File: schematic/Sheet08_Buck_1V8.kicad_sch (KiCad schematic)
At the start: 15 parts, among them U6 ISL70003ASEH

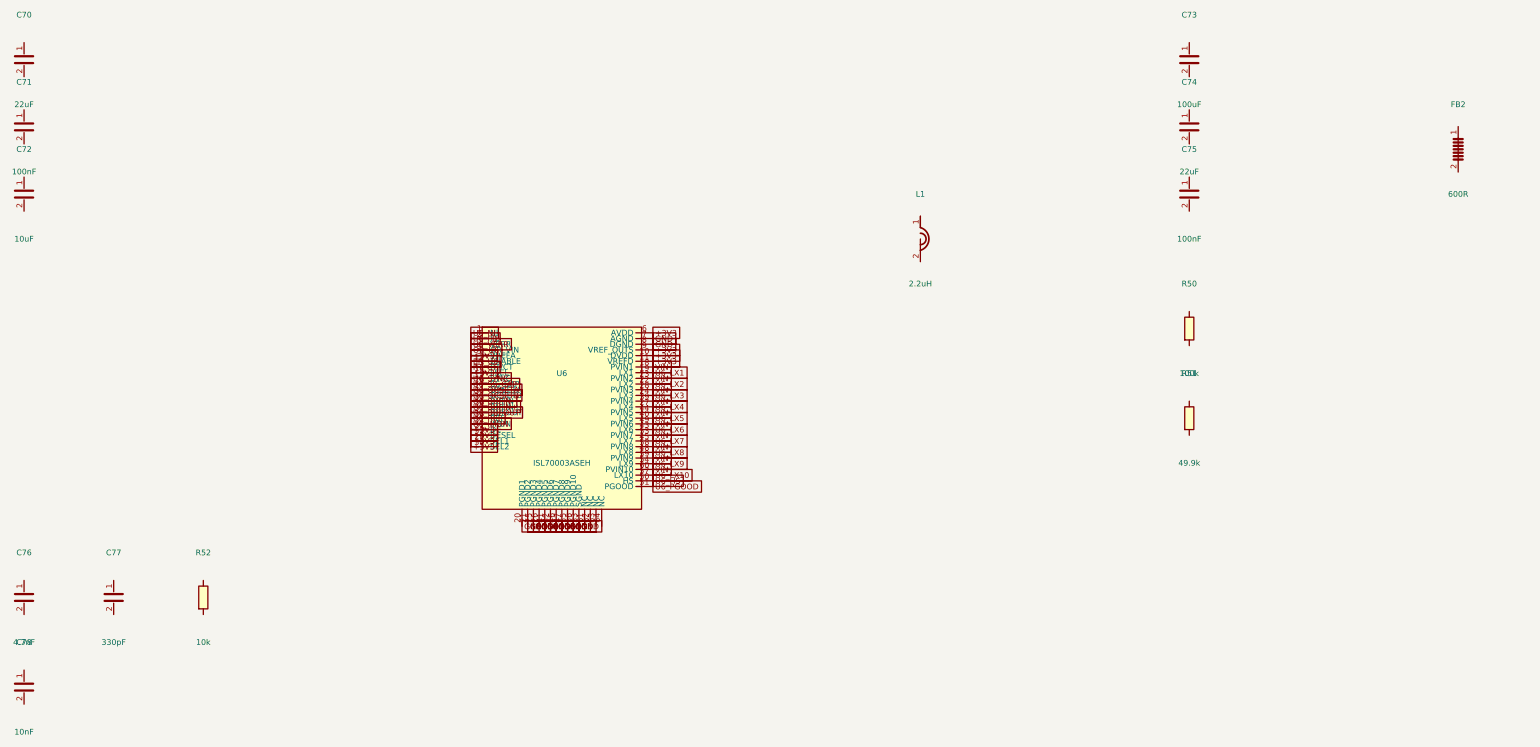
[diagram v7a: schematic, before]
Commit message: feat: connect ALL passive components and fix clock routing
- Added PASSIVE_TOPOLOGY dict mapping 139 passives to their nets
- Passive pin endpoints now get global_labels (was 0 connected, now 138)
- R38 intentionally GND-GND (RECAL_EN pull-down)
- Fixed LMK clock output mapping: CLKout0→ADC_CLK_P, CLKout2→FPGA_REFCLK_P, etc.
- Fixed TPS7H5001-SP SYNC pin collision with LMX_SYNC
- Total connections: 867 pins (up from 641)
- Cross-sheet nets: 52
- Power rails: VIN(33), +3V3(98), GND(228) all with decoupling
- JESD204C: U1↔U2 on 4 lanes ✓
- SPI: U1↔U2↔U3↔U4 ✓
- Clock: LMK→ADC (CLK+SYSREF), LMK→FPGA (REF+SPW) ✓
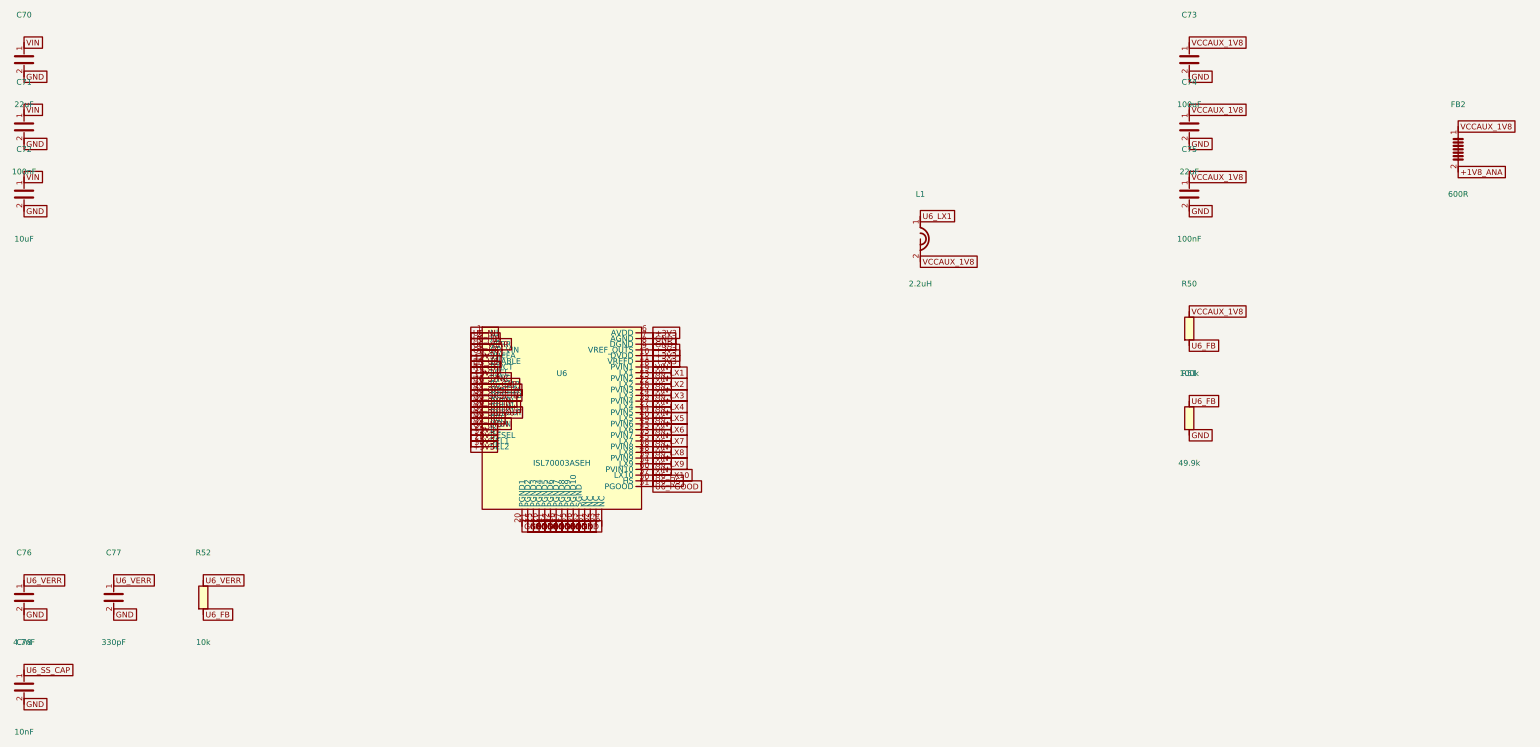
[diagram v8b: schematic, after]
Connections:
- net GND: now also C70.2, C71.2, C72.2, C73.2, C74.2, C75.2, C76.2, C77.2, C78.2, R51.2
- net U6_FB: now also R50.2, R51.1, R52.2
- net U6_LX1: now also L1.1
- net U6_SS_CAP: now also C78.1
- net U6_VERR: now also C76.1, C77.1, R52.1
- net VIN: now also C70.1, C71.1, C72.1
- net VCCAUX_1V8: now reaches C73.1
- net VCCAUX_1V8: now also C74.1, C75.1, FB2.1, L1.2, R50.1
- net +1V8_ANA: now reaches FB2.2
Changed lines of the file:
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@@
   (global_label "GND" (at 202.5400 144.1300 0) (effects (font (size 1.27 1.27))))
   (global_label "GND" (at 203.8100 144.1300 0) (effects (font (size 1.27 1.27))))
+  (global_label "VIN" (at 80.0000 36.1900 0) (effects (font (size 1.27 1.27))))
+  (global_label "GND" (at 80.0000 43.8100 0) (effects (font (size 1.27 1.27))))
+  (global_label "VIN" (at 80.0000 51.1900 0) (effects (font (size 1.27 1.27))))
+  (global_label "GND" (at 80.0000 58.8100 0) (effects (font (size 1.27 1.27))))
+  (global_label "VIN" (at 80.0000 66.1900 0) (effects (font (size 1.27 1.27))))
+  (global_label "GND" (at 80.0000 73.8100 0) (effects (font (size 1.27 1.27))))
+  (global_label "U6_LX1" (at 280.0000 74.9200 0) (effects (font (size 1.27 1.27))))
+  (global_label "VCCAUX_1V8" (at 280.0000 85.0800 0) (effects (font (size 1.27 1.27))))
+  (global_label "VCCAUX_1V8" (at 340.0000 36.1900 0) (effects (font (size 1.27 1.27))))
+  (global_label "GND" (at 340.0000 43.8100 0) (effects (font (size 1.27 1.27))))
+  (global_label "VCCAUX_1V8" (at 340.0000 51.1900 0) (effects (font (size 1.27 1.27))))
+  (global_label "GND" (at 340.0000 58.8100 0) (effects (font (size 1.27 1.27))))
+  (global_label "VCCAUX_1V8" (at 340.0000 66.1900 0) (effects (font (size 1.27 1.27))))
+  (global_label "GND" (at 340.0000 73.8100 0) (effects (font (size 1.27 1.27))))
+  (global_label "VCCAUX_1V8" (at 340.0000 96.1900 0) (effects (font (size 1.27 1.27))))
+  (global_label "U6_FB" (at 340.0000 103.8100 0) (effects (font (size 1.27 1.27))))
+  (global_label "U6_FB" (at 340.0000 116.1900 0) (effects (font (size 1.27 1.27))))
+  (global_label "GND" (at 340.0000 123.8100 0) (effects (font (size 1.27 1.27))))
+  (global_label "U6_VERR" (at 80.0000 156.1900 0) (effects (font (size 1.27 1.27))))
+  (global_label "GND" (at 80.0000 163.8100 0) (effects (font (size 1.27 1.27))))
+  (global_label "U6_VERR" (at 100.0000 156.1900 0) (effects (font (size 1.27 1.27))))
+  (global_label "GND" (at 100.0000 163.8100 0) (effects (font (size 1.27 1.27))))
+  (global_label "U6_VERR" (at 120.0000 156.1900 0) (effects (font (size 1.27 1.27))))
+  (global_label "U6_FB" (at 120.0000 163.8100 0) (effects (font (size 1.27 1.27))))
+  (global_label "U6_SS_CAP" (at 80.0000 176.1900 0) (effects (font (size 1.27 1.27))))
+  (global_label "GND" (at 80.0000 183.8100 0) (effects (font (size 1.27 1.27))))
+  (global_label "VCCAUX_1V8" (at 400.0000 54.9200 0) (effects (font (size 1.27 1.27))))
+  (global_label "+1V8_ANA" (at 400.0000 65.0800 0) (effects (font (size 1.27 1.27))))
   (sheet_instances (path "/" (page "1")))
 )
